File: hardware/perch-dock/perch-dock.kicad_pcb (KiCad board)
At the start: 2 copper layers, 0 parts

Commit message: feat(hardware): lay out and route the perch board with the snap-off dock-pad section; perch DRC clean
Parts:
- added C1: 10uF, Capacitor_SMD:C_0603_1608Metric, F.Cu at (102.4, 95.9)
- added C2: 100nF, Capacitor_SMD:C_0402_1005Metric, F.Cu at (102.4, 104.2)
- added D1: SMF5.0A, Diode_SMD:D_SOD-123F, F.Cu at (106.5, 95.4)
- added D2: LESD5D5.0CT1G, Diode_SMD:D_SOD-523, F.Cu at (93.0, 104.6)
- added F1: 1.1A hold, Fuse:Fuse_1206_3216Metric, F.Cu at (100.0, 94.0)
- added H1: M2, MountingHole:MountingHole_2.2mm_M2, F.Cu at (86.0, 95.0)
- added H2: M2, MountingHole:MountingHole_2.2mm_M2, F.Cu at (86.0, 105.0)
- added J1: USB-C power, Connector_USB:USB_C_Receptacle_HRO_TYPE-C-31-M-12, F.Cu at (113.8, 100.0)
- added J2: To J303: GND, VBUS, DET, GND, Connector_JST:JST_SH_SM04B-SRSS-TB_1x04-1MP_P1.00mm_Horizontal, F.Cu at (110.0, 117.0)
- added LED1: red, LED_SMD:LED_0603_1608Metric, F.Cu at (91.0, 94.4)
- added MB1: Breakaway, owltunes:MouseBite_2.5mm_2x0.6mm, F.Cu at (100.0, 108.6)
- added MB2: Breakaway, owltunes:MouseBite_2.5mm_2x0.6mm, F.Cu at (100.0, 112.4)
- added P1: Pogo DET, owltunes:PogoPin_Xinyangze_YZ71215080P-02, F.Cu at (95.5, 100.0)
- added P2: Pogo GND, owltunes:PogoPin_Xinyangze_YZ71215080P-02, F.Cu at (100.0, 100.0)
- added P3: Pogo VBUS, owltunes:PogoPin_Xinyangze_YZ71215080P-02, F.Cu at (104.5, 100.0)
- added PAD1: DET, TestPoint:TestPoint_Pad_D3.0mm, B.Cu at (95.5, 116.5)
- added PAD2: GND, TestPoint:TestPoint_Pad_D3.0mm, B.Cu at (100.0, 116.5)
- added PAD3: VBUS, TestPoint:TestPoint_Pad_D3.0mm, B.Cu at (104.5, 116.5)
- added R1: 5.1k, Resistor_SMD:R_0402_1005Metric, F.Cu at (107.2, 101.2)
- added R2: 5.1k, Resistor_SMD:R_0402_1005Metric, F.Cu at (107.2, 98.9)
- added R3: 10k, Resistor_SMD:R_0402_1005Metric, F.Cu at (93.0, 102.6)
- added R4: 4.7k, Resistor_SMD:R_0402_1005Metric, F.Cu at (91.0, 96.6)
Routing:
- net VBUS_OUT: track 0.00 -> 26.4 mm
- net PAD_GND: track 0.00 -> 25.6 mm, vias 0 -> 1
- net VBUS_IN: track 0.00 -> 18.3 mm, vias 0 -> 2
- net PAD_DET: track 0.00 -> 12.5 mm, vias 0 -> 1
- net GND: track 0.00 -> 11.0 mm, vias 0 -> 6
- net DOCK_ID: track 0.00 -> 7.62 mm
- net PAD_VBUS: track 0.00 -> 5.47 mm, vias 0 -> 1
- net PERCH_CC1: track 0.00 -> 2.62 mm
- net PERCH_CC2: track 0.00 -> 2.56 mm
- net LED_A: track 0.00 -> 2.24 mm
- added copper zone on B.Cu, net GND
- added copper zone on F.Cu, net GND
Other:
- board outline added: 34 x 29 mm
- board text added: "CERN-OHL-P-2.0"
- board text added: "DET"
- board text added: "GND"
- board text added: "J2 to J303, pin 1 to pin 1"
- board text added: "OWL DOCK PADS"
- board text added: "OwlTunes perch rev A"
- board text added: "VBUS"

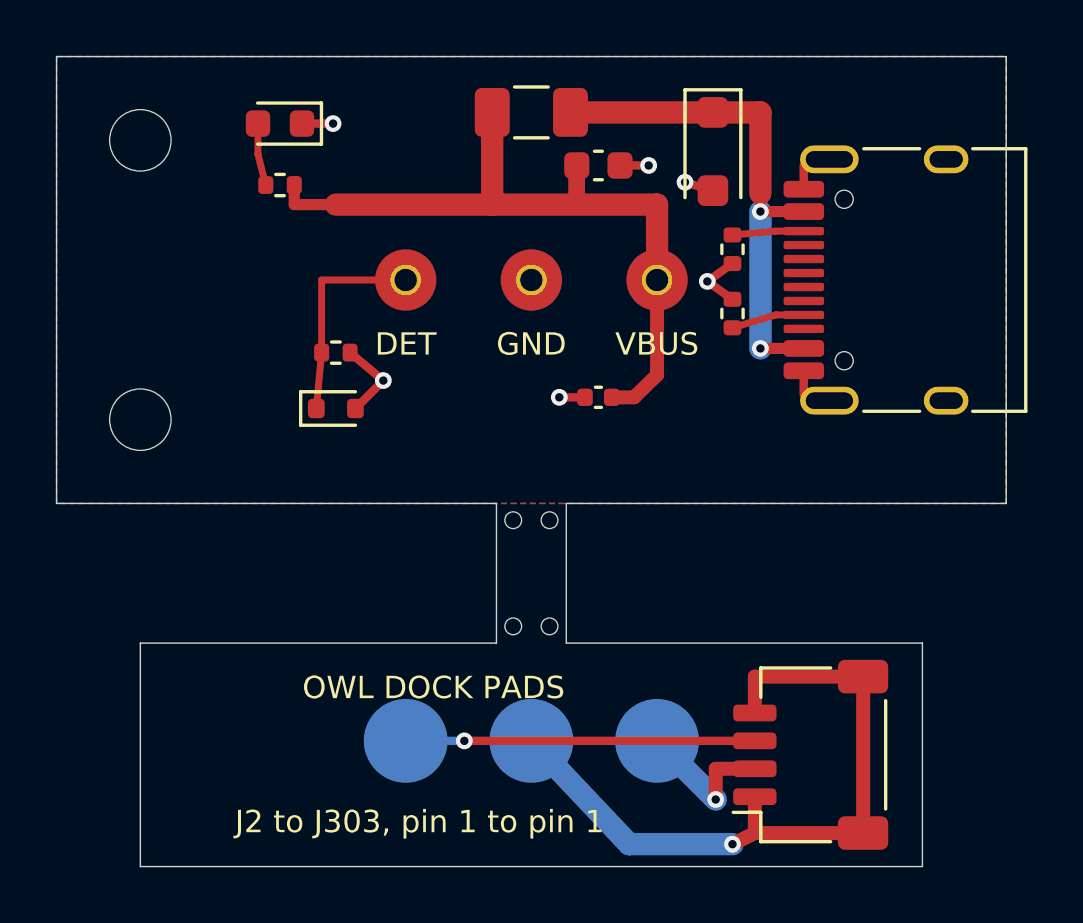
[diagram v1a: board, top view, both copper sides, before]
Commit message: fix(hardware): put the perch mouse bites on the neck edges and move J1 1.5 mm down for a full-size USB-C plug
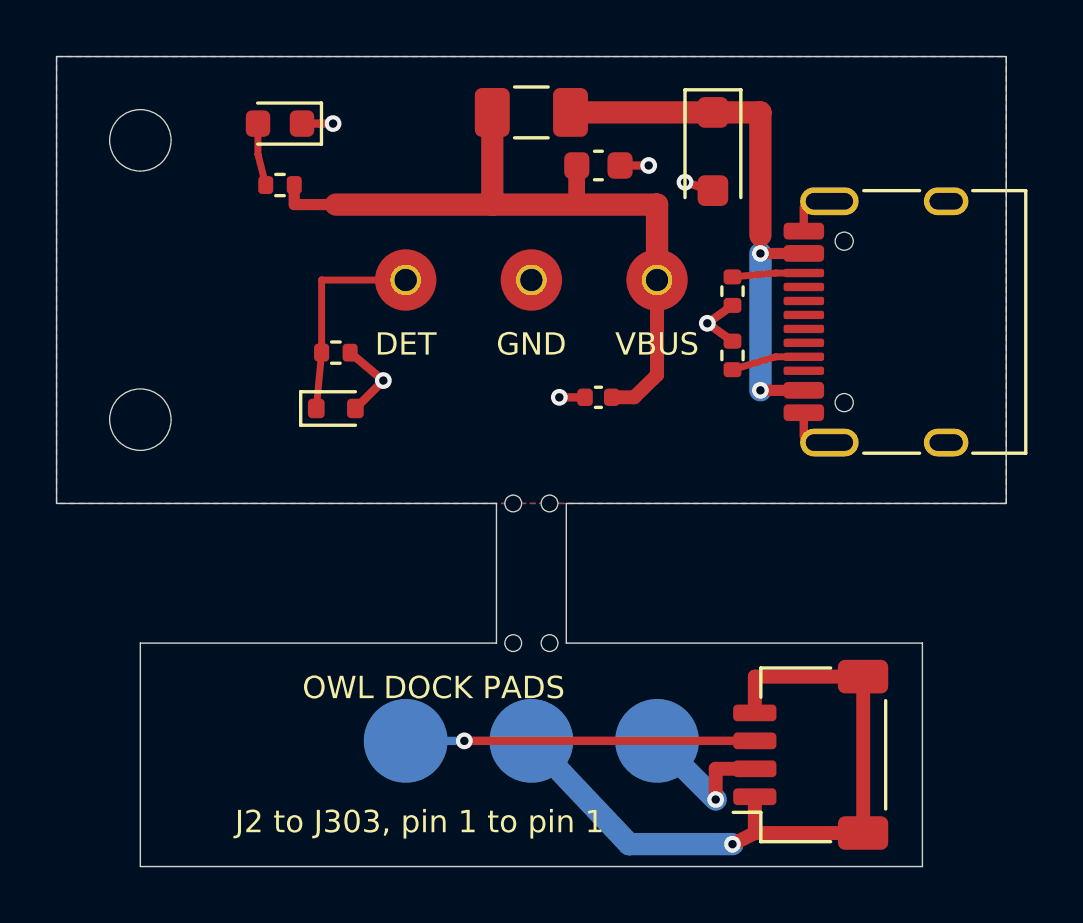
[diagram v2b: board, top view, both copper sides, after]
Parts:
- moved J1 1.50 mm to (113.8, 101.5)
- moved R1 1.50 mm to (107.2, 102.7)
- moved R2 1.50 mm to (107.2, 100.4)
- moved MB1 0.60 mm to (100.0, 108.0)
- moved MB2 0.60 mm to (100.0, 113.0)
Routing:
- net VBUS_IN: track 18.3 -> 19.8 mm
